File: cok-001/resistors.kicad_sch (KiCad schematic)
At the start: 56 parts, among them Q1101 DTC144E, Q1102 DTC144E, U1101 ADT7461A0002RMZR

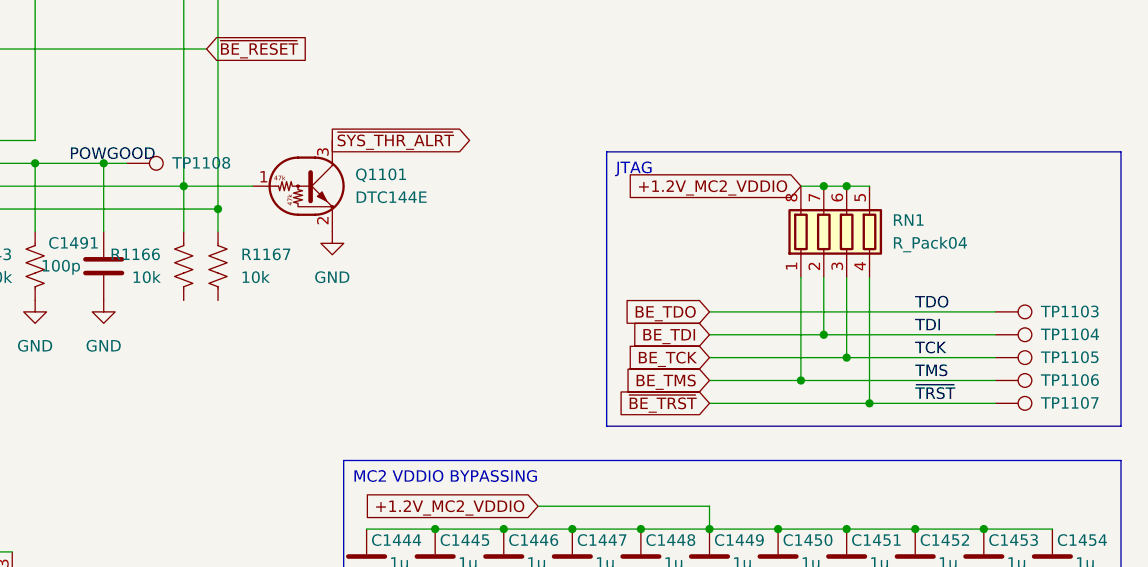
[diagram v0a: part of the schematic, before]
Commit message: added hdmi and jtag
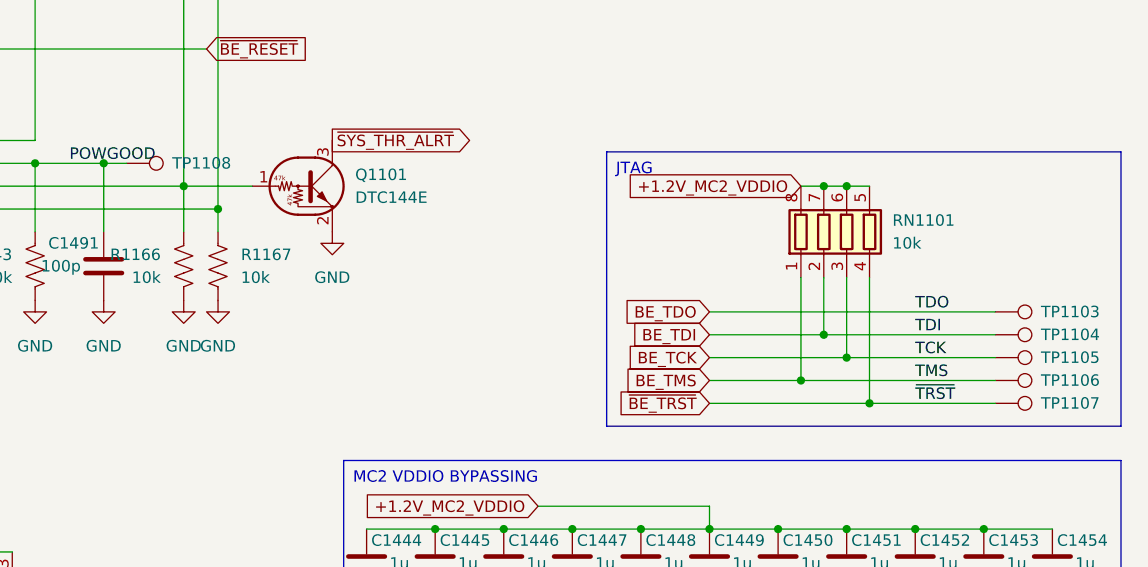
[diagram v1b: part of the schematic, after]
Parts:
- Q1101, Q1102: footprint (none) -> Package_TO_SOT_SMD:SOT-323_SC-70
- RN1101: renamed from RN1; value R_Pack04 -> 10k; footprint (none) -> Resistor_SMD:R_Array_Convex_4x0402
- TP1103, TP1104, TP1105, TP1106, TP1107: footprint (none) -> TestPoint:TestPoint_Pad_1.0x1.0mm
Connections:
- net GND: now also R1166.1, R1167.1
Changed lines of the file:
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@@
 			)
 		)
-		(property "Footprint" ""
+		(property "Footprint" "TestPoint:TestPoint_Pad_1.0x1.0mm"
 			(at 267.97 73.66 0)
 			(effects
@@
 		(dnp no)
 		(fields_autoplaced yes)
-		(property "Reference" "RN1"
+		(property "Reference" "RN1101"
 			(at 256.54 48.2599 0)
 			(effects
@@
 			)
 		)
-		(property "Value" "R_Pack04"
+		(property "Value" "10k"
 			(at 256.54 50.7999 0)
 			(effects
@@
 			)
 		)
-		(property "Footprint" ""
+		(property "Footprint" "Resistor_SMD:R_Array_Convex_4x0402"
 			(at 258.445 49.53 90)
 			(effects
@@
 			(project ""
 				(path "/976eb78d-8215-4cc0-9d72-f9d535c7970b/edea7873-2074-40c6-a93e-4af210829a02"
-					(reference "RN1")
+					(reference "RN1101")
 					(unit 1)
 				)
@@
 			)
 		)
-		(property "Footprint" ""
+		(property "Footprint" "Package_TO_SOT_SMD:SOT-323_SC-70"
 			(at 161.29 90.17 0)
 			(effects
@@
 			)
 		)
-		(property "Footprint" ""
+		(property "Footprint" "TestPoint:TestPoint_Pad_1.0x1.0mm"
 			(at 267.97 66.04 0)
 			(effects
@@
 			)
 		)
-		(property "Footprint" ""
+		(property "Footprint" "TestPoint:TestPoint_Pad_1.0x1.0mm"
 			(at 267.97 71.12 0)
 			(effects
@@
 	)
 	(symbol
+		(lib_id "power:GND")
+		(at 177.8 57.15 0)
+		(mirror y)
+		(unit 1)
+		(exclude_from_sim no)
+		(in_bom yes)
+		(on_board yes)
+		(dnp no)
+		(fields_autoplaced yes)
+		(property "Reference" "#PWR0172"
+			(at 177.8 63.5 0)
+			(effects
+				(font
+					(size 1.27 1.27)
+				)
+				(hide yes)
+			)
+		)
+		(property "Value" "GND"
+			(at 177.8 62.23 0)
+			(effects
+				(font
+					(size 1.27 1.27)
+				)
+			)
+		)
+		(property "Footprint" ""
+			(at 177.8 57.15 0)
+			(effects
+				(font
+					(size 1.27 1.27)
+				)
+				(hide yes)
+			)
+		)
+		(property "Datasheet" ""
+			(at 177.8 57.15 0)
+			(effects
+				(font
+					(size 1.27 1.27)
+				)
+				(hide yes)
+			)
+		)
+		(property "Description" "Power symbol creates a global label with name \"GND\" , ground"
+			(at 177.8 57.15 0)
+			(effects
+				(font
+					(size 1.27 1.27)
+				)
+				(hide yes)
+			)
+		)
+		(pin "1"
+		)
+		(instances
+			(project "cok-001"
+				(path "/976eb78d-8215-4cc0-9d72-f9d535c7970b/edea7873-2074-40c6-a93e-4af210829a02"
+					(reference "#PWR0172")
+					(unit 1)
+				)
+			)
+		)
+	)
+	(symbol
 		(lib_id "Device:R_US")
 		(at 181.61 53.34 180)
@@
 	)
 	(symbol
+		(lib_id "power:GND")
+		(at 181.61 57.15 0)
+		(mirror y)
+		(unit 1)
+		(exclude_from_sim no)
+		(in_bom yes)
+		(on_board yes)
+		(dnp no)
+		(fields_autoplaced yes)
+		(property "Reference" "#PWR0173"
+			(at 181.61 63.5 0)
+			(effects
+				(font
+					(size 1.27 1.27)
+				)
+				(hide yes)
+			)
+		)
+		(property "Value" "GND"
+			(at 181.61 62.23 0)
+			(effects
+				(font
+					(size 1.27 1.27)
+				)
+			)
+		)
+		(property "Footprint" ""
+			(at 181.61 57.15 0)
+			(effects
+				(font
+					(size 1.27 1.27)
+				)
+				(hide yes)
+			)
+		)
+		(property "Datasheet" ""
+			(at 181.61 57.15 0)
+			(effects
+				(font
+					(size 1.27 1.27)
+				)
+				(hide yes)
+			)
+		)
+		(property "Description" "Power symbol creates a global label with name \"GND\" , ground"
+			(at 181.61 57.15 0)
+			(effects
+				(font
+					(size 1.27 1.27)
+				)
+				(hide yes)
+			)
+		)
+		(pin "1"
+		)
+		(instances
+			(project "cok-001"
+				(path "/976eb78d-8215-4cc0-9d72-f9d535c7970b/edea7873-2074-40c6-a93e-4af210829a02"
+					(reference "#PWR0173")
+					(unit 1)
+				)
+			)
+		)
+	)
+	(symbol
 		(lib_id "Device:C")
 		(at 220.98 86.36 0)
@@
 			)
 		)
-		(property "Footprint" ""
+		(property "Footprint" "Package_TO_SOT_SMD:SOT-323_SC-70"
 			(at 191.77 44.45 0)
 			(effects
@@
 			)
 		)
-		(property "Footprint" ""
+		(property "Footprint" "TestPoint:TestPoint_Pad_1.0x1.0mm"
 			(at 267.97 63.5 0)
 			(effects
@@
 			)
 		)
-		(property "Footprint" ""
+		(property "Footprint" "TestPoint:TestPoint_Pad_1.0x1.0mm"
 			(at 267.97 68.58 0)
 			(effects

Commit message: sata
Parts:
- TP1101, TP1102, TP1108, TP1119, TP1120: footprint (none) -> TestPoint:TestPoint_Pad_1.0x1.0mm
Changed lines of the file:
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@@
 			)
 		)
-		(property "Footprint" ""
+		(property "Footprint" "TestPoint:TestPoint_Pad_1.0x1.0mm"
 			(at 171.45 46.99 0)
 			(effects
@@
 			)
 		)
-		(property "Footprint" ""
+		(property "Footprint" "TestPoint:TestPoint_Pad_1.0x1.0mm"
 			(at 52.07 68.58 0)
 			(effects
@@
 			)
 		)
-		(property "Footprint" ""
+		(property "Footprint" "TestPoint:TestPoint_Pad_1.0x1.0mm"
 			(at 52.07 38.1 0)
 			(effects
@@
 			)
 		)
-		(property "Footprint" ""
+		(property "Footprint" "TestPoint:TestPoint_Pad_1.0x1.0mm"
 			(at 134.62 29.21 0)
 			(effects
@@
 			)
 		)
-		(property "Footprint" ""
+		(property "Footprint" "TestPoint:TestPoint_Pad_1.0x1.0mm"
 			(at 152.4 29.21 0)
 			(effects

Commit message: sc
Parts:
- added C1106: 1u, Capacitor_SMD:C_0402_1005Metric, symbol Device:C
- added C1117: 270p, Capacitor_SMD:C_0402_1005Metric, symbol Device:C
- added C1136, C1137, C1152, C1153, C1154, C1155: 0.1u, Capacitor_SMD:C_0402_1005Metric, symbol Device:C
- added C1160: 0.01u, Capacitor_SMD:C_0402_1005Metric, symbol Device:C
- added L1101: 270nH, Inductor_SMD:L_0603_1608Metric, symbol Device:L
- added R1108, R1109, R1118, R1119, R1120, R1121: 49.9, Resistor_SMD:R_0402_1005Metric, symbol Device:R_US
- added R1112, R1114: 95.3, Resistor_SMD:R_0402_1005Metric, symbol Device:R_US
- added R1113, R1115: 191, Resistor_SMD:R_0402_1005Metric, symbol Device:R_US
- added R1116, R1155, R1157, R1159, R1161, R1162, R1163: 100, Resistor_SMD:R_0402_1005Metric, symbol Device:R_US
- added R1152, R1158, R1160, R1169: 10k, Resistor_SMD:R_0402_1005Metric, symbol Device:R_US
- added R1170: 0, Resistor_SMD:R_0402_1005Metric, symbol Device:R_US
- added TP1117, TP1118: TestPoint, TestPoint:TestPoint_Pad_1.0x1.0mm, symbol Connector:TestPoint
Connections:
- net +1.2V_MC2_VDDIO: now also R1152.2, R1158.2, R1160.2, R1169.2
- net +1.2V_YC_RC_VDDIO: now also C1136.1, C1137.1, C1152.1, C1153.1, C1154.1, C1155.1, R1108.2, R1109.2, R1112.2, R1114.2, R1118.2, R1119.2, R1120.2, R1121.2
- net GND: now also C1106.2, C1117.2, C1152.2, C1153.2, C1154.2, C1155.2, C1160.2, R1116.1, R1155.1, R1157.1, R1159.1, R1161.1, R1162.2, R1163.2
- new net +1.5V_BE_THERMAL_VDDA: C1160.1, R1170.2
- new net +1.6V_BE_VDDA: L1101.1
- new net BE_PLL_VDDA: C1106.1, C1117.1, L1101.2, R1170.1
- new net BE_P_L_BYPASS: R1169.1
- new net BE_SCAN_ENA: R1116.2
- new net BE_SPI_CTL0: R1162.1
- new net BE_SPI_CTL1: R1163.1
- new net BE_SYS_CONF0: R1155.2
- new net BE_SYS_CONF1: R1157.2
- new net BE_SYS_CONF2: R1158.1, R1159.2
- new net BE_SYS_CONF3: R1160.1, R1161.2
- new net BE_TBEN: R1152.1
- new net BE_Y0_DQ0_RLOAD: R1118.1
- new net BE_Y0_DQ2_RLOAD: R1120.1
- new net BE_Y0_DQC_ROLREF: R1108.1
- new net BE_Y0_DQC_VOLGND: C1136.2, R1113.1
- new net BE_Y0_DQC_VOLREF: R1112.1, R1113.2, TP1117.1
- new net BE_Y1_DQ0_RLOAD: R1119.1
- new net BE_Y1_DQ2_RLOAD: R1121.1
- new net BE_Y1_DQC_ROLREF: R1109.1
- new net BE_Y1_DQC_VOLGND: C1137.2, R1115.1
- new net BE_Y1_DQC_VOLREF: R1114.1, R1115.2, TP1118.1

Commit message: msop
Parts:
- U1101: footprint Package_SO:MSOP-8_3x3mm_P0.65mm -> PS3:MSOP-8_2.9x4mm_P0.65mm
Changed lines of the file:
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@@
 			)
 		)
-		(property "Footprint" "Package_SO:MSOP-8_3x3mm_P0.65mm"
+		(property "Footprint" "PS3:MSOP-8_2.9x4mm_P0.65mm"
 			(at 250.19 119.38 0)
 			(effects

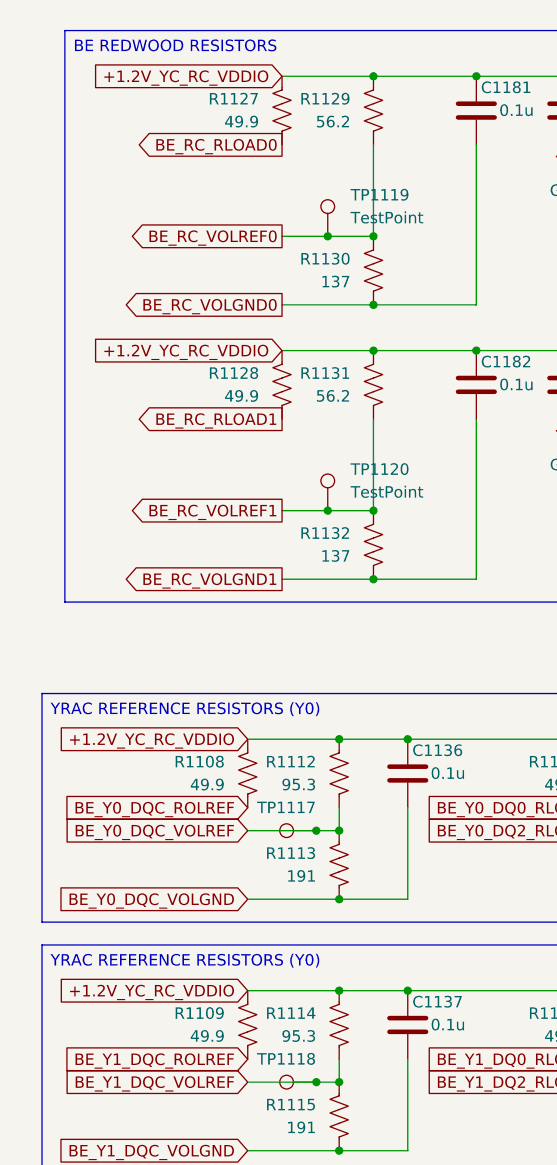
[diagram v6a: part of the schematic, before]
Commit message: power flags
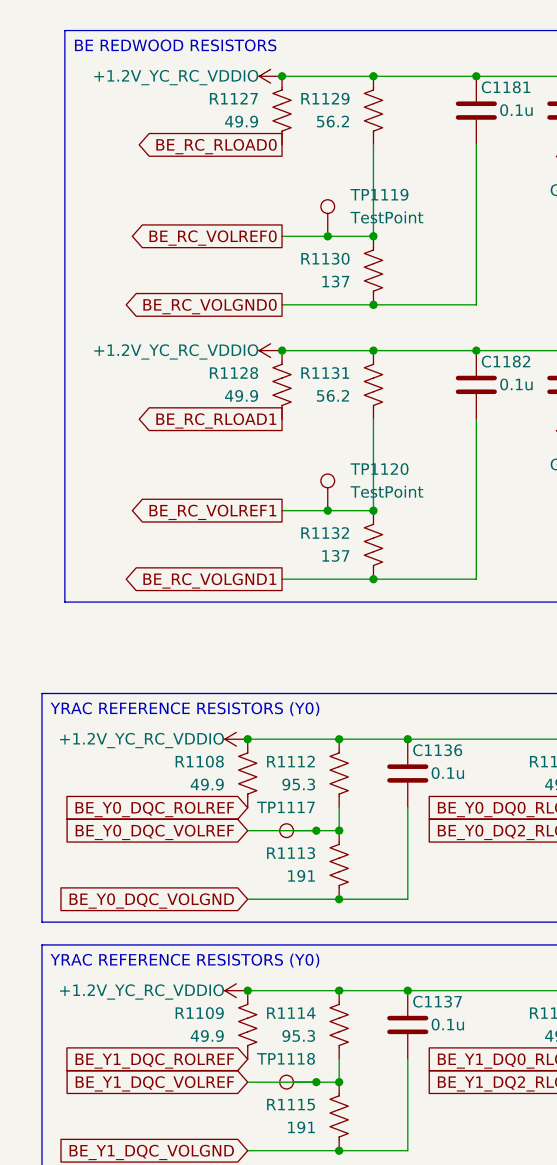
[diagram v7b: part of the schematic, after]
